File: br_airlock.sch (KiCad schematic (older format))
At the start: 23 parts, among them P1 Digital, P2 Analog, P3 CONN_01X01, P4 CONN_01X01, P5 CONN_01X01, P6 CONN_01X01

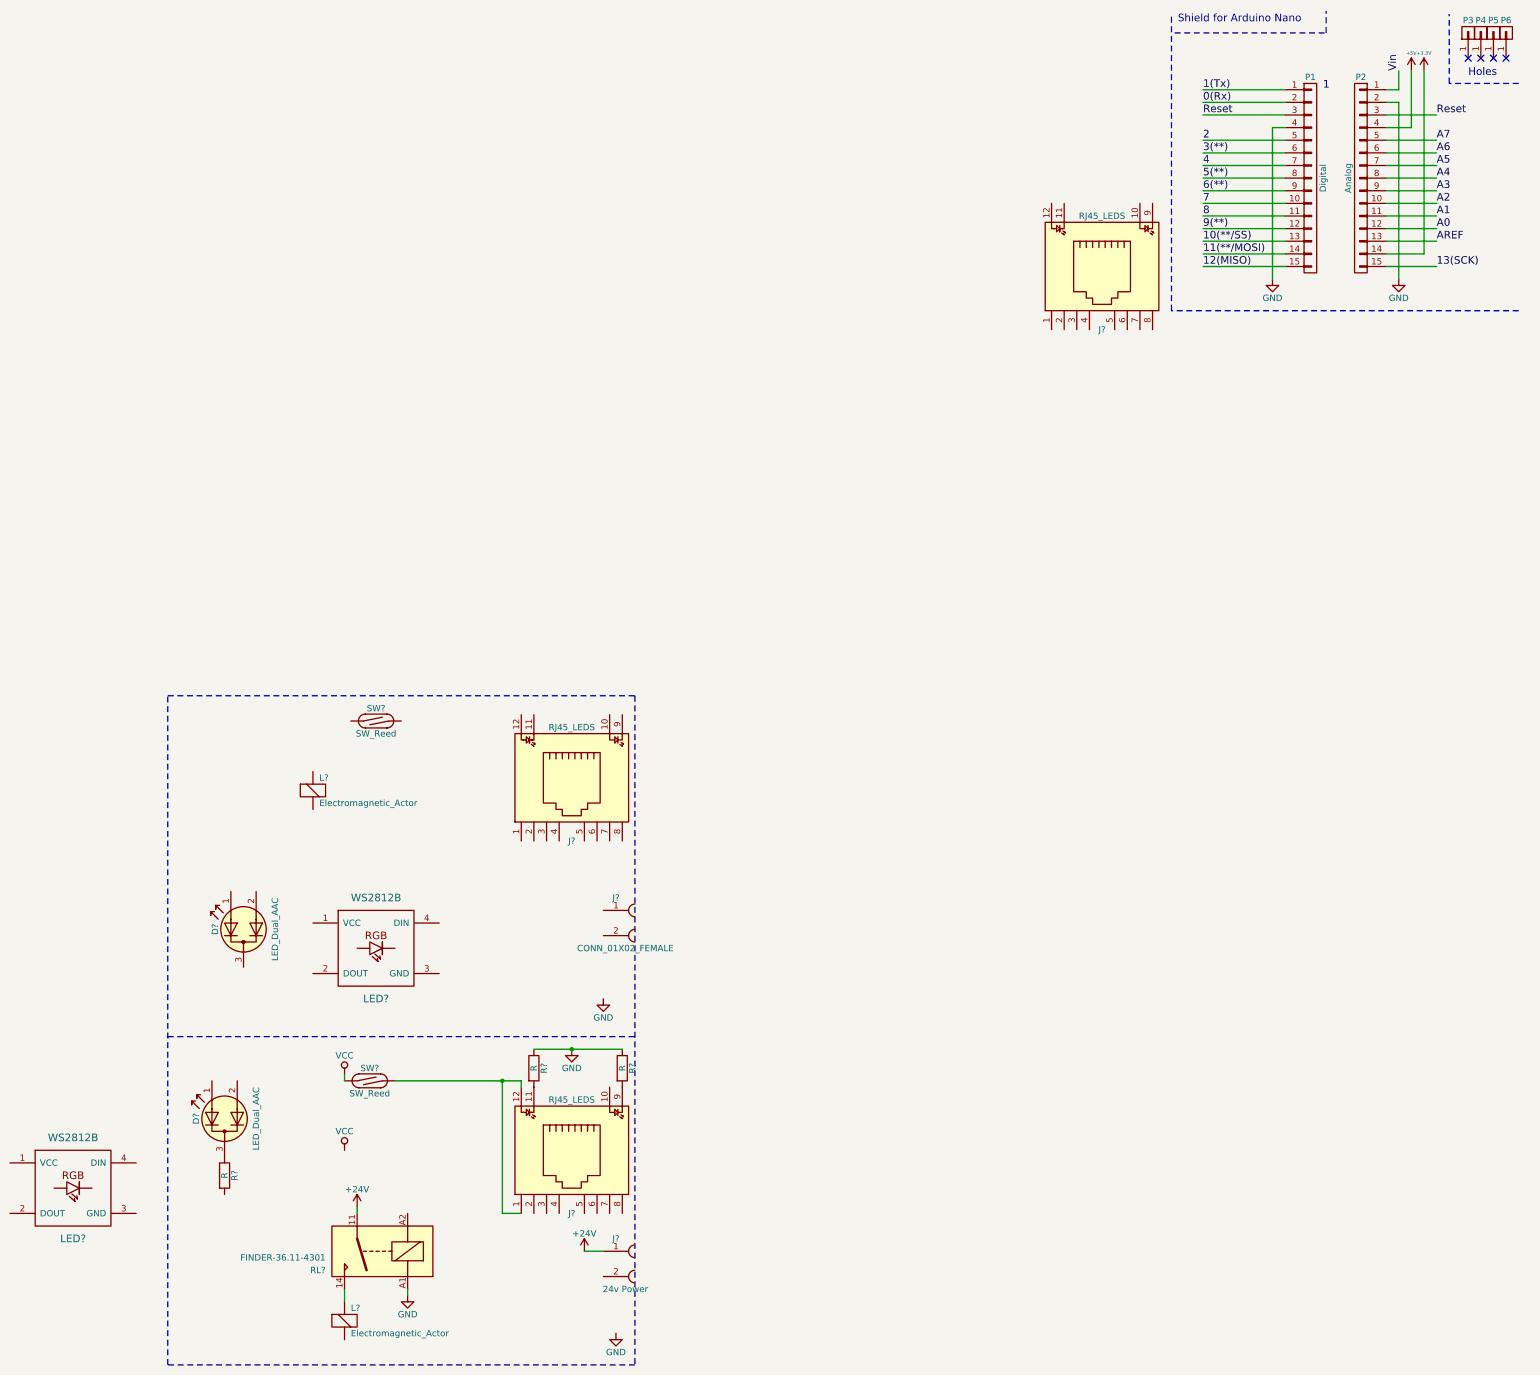
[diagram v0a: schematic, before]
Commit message: More additions. Thinking I'm running out of pins on the RJ45s, might look into a simple i/o expander.
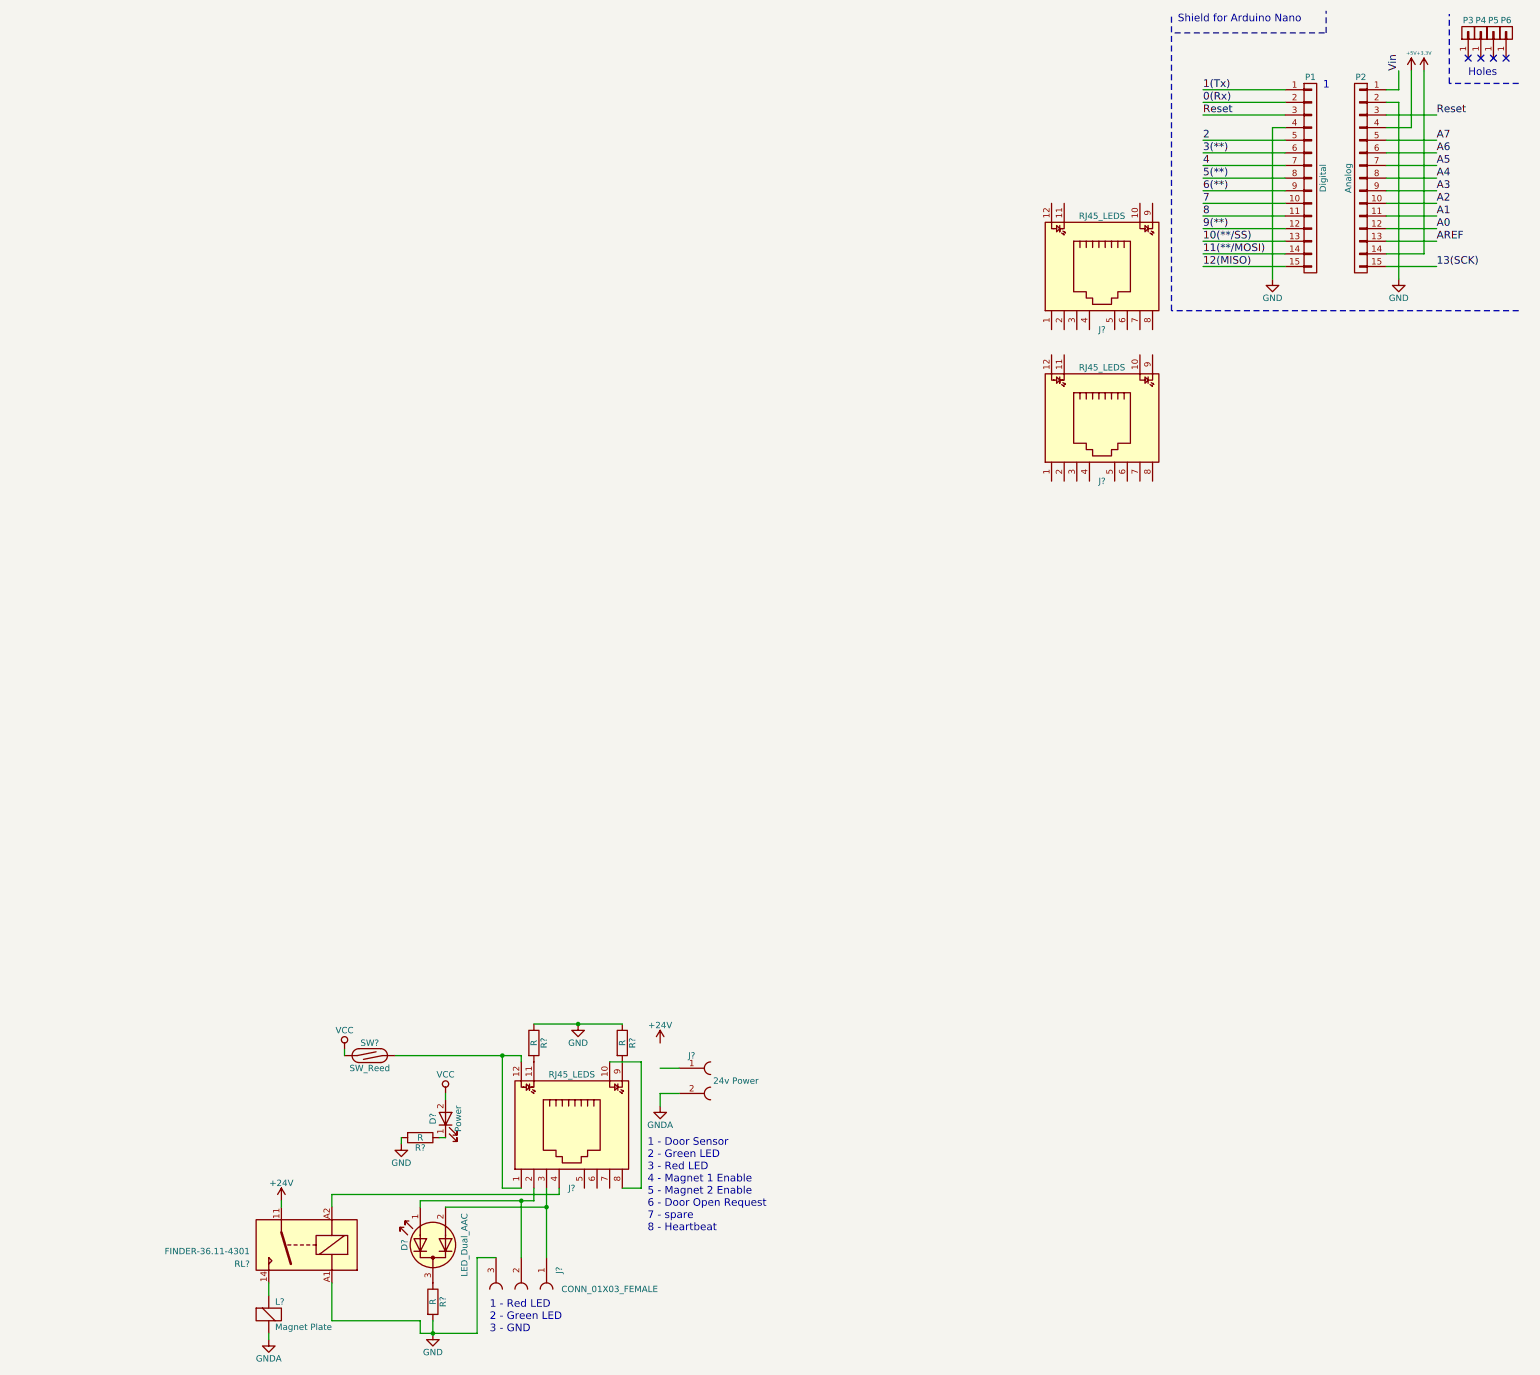
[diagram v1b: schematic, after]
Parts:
- removed D?: LED_Dual_AAC, symbol LED_Dual_AAC
- removed J?: RJ45_LEDS, symbol RJ45_LEDS
- removed J?: CONN_01X02_FEMALE, symbol CONN_01X02_FEMALE
- removed L?: Electromagnetic_Actor, symbol Electromagnetic_Actor
- removed LED? (x2): WS2812B, symbol WS2812B
- removed SW?: SW_Reed, symbol SW_Reed
- added D?: Power, symbol LED
- added J?: RJ45_LEDS, symbol RJ45_LEDS
- added J?: CONN_01X03_FEMALE, symbol CONN_01X03_FEMALE
- added R?: R, symbol R
- L?: value Electromagnetic_Actor -> Magnet Plate
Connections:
- net +24V: no longer J?.1
- net GND: now also R?.2, J?.3, R?.2
- net VCC: now also D?.2 (A)
- net GNDA: now reaches L?.2 (+)
- net GNDA: now also J?.2
- net at J?.10: now also J?.8
- net at J?.2: now also D?.1 (A1), J?.2
- net at J?.3: now also D?.2 (A2), J?.1
- net at J?.4: now also RL?.A2
- new net: D?.1 (K), R?.1
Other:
- note added: "1 - Door Sensor\n2 - Green LED\n3 - Red LED\n4 - Magnet 1 Enable\n5 - Magnet 2 Enable\n6 - Door Open Request\n7 - spare\n8 - Heartbeat"
- note added: "1 - Red LED\n2 - Green LED\n3 - GND"
- moved on the sheet: D?, J?, L?, R?, RL?, SW?

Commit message: Switched to a PCF8754 I/O Expander. Kinda wanted to always play with one.
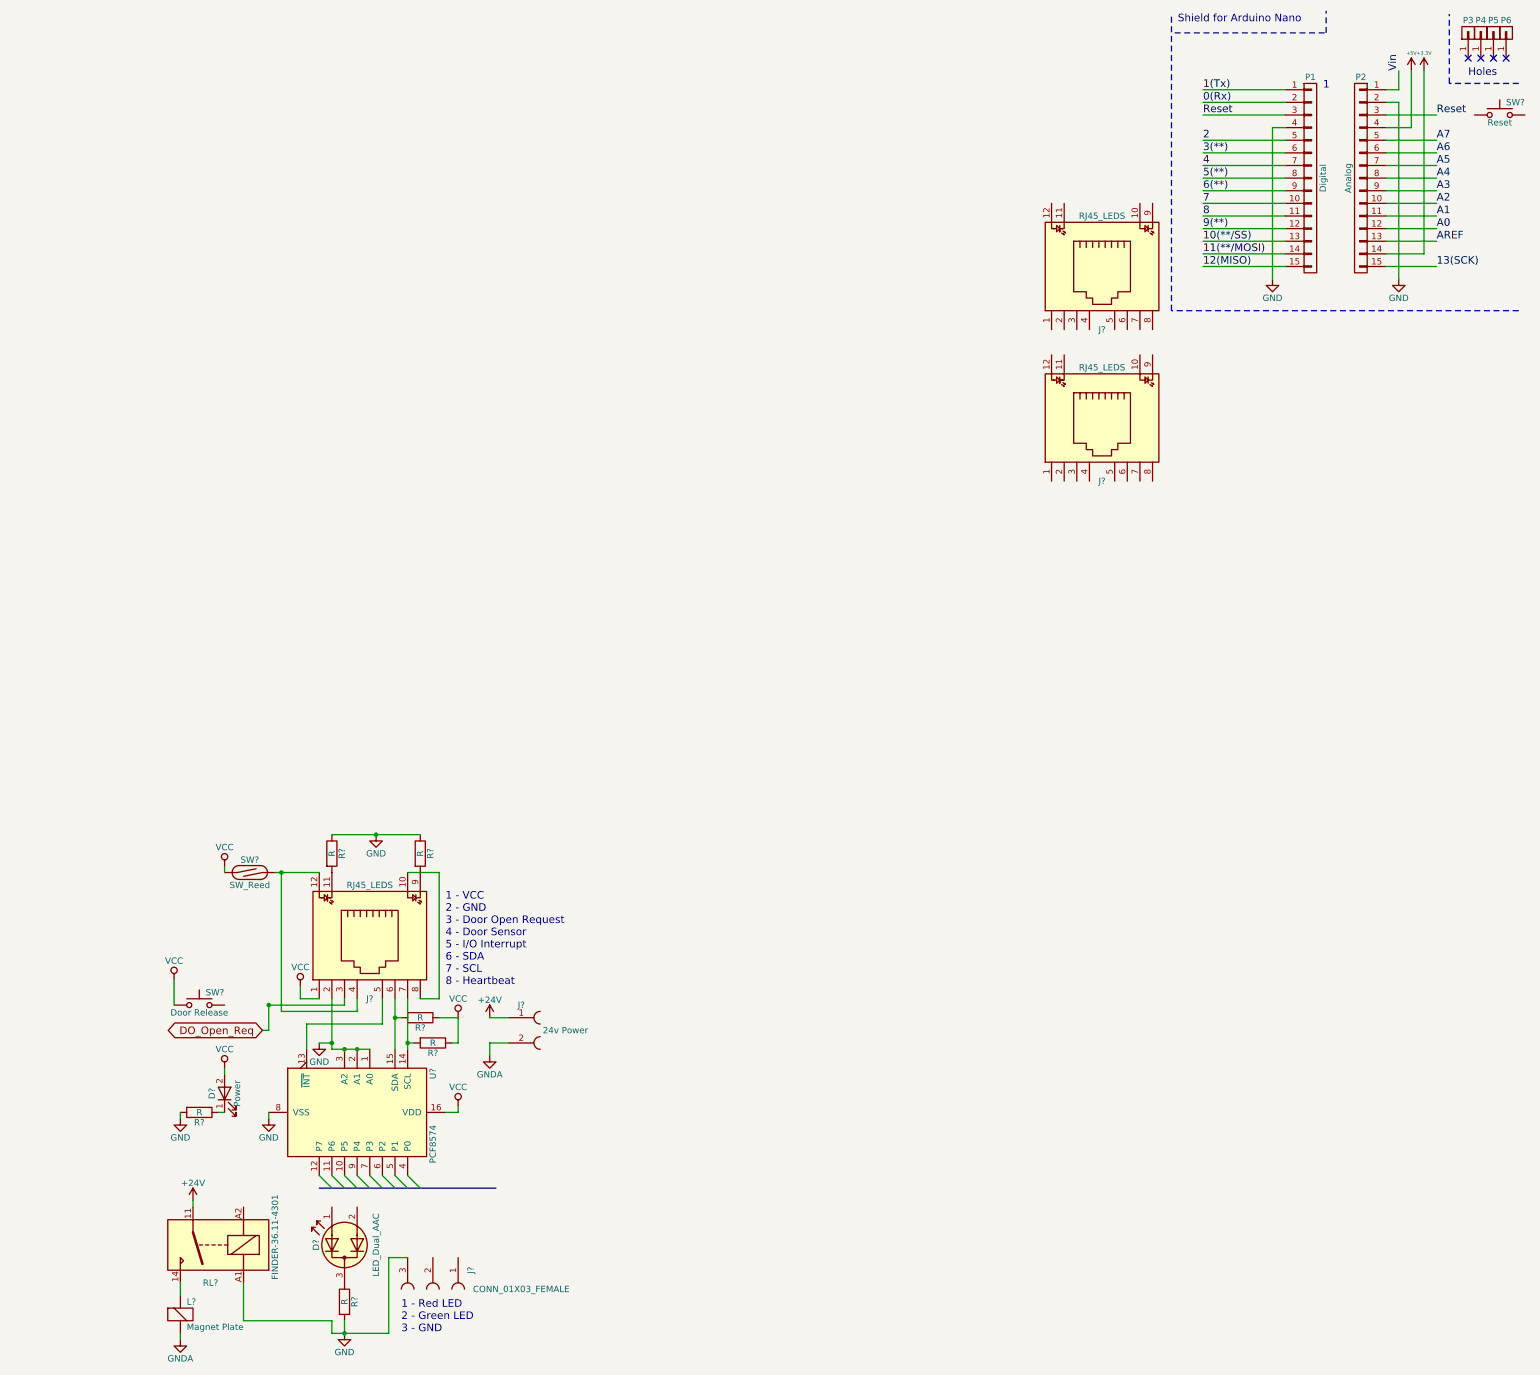
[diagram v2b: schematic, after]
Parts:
- added R? (x2): R, symbol R
- added SW?: Door Release, symbol SW_Push
- added SW?: Reset, symbol SW_Push
- added U?: PCF8574, symbol PCF8574
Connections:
- net +24V: now also J?.1
- net GND: now also J?.2, U?.1 (A0), U?.2 (A1), U?.3 (A2), U?.8 (VSS)
- net VCC: now also J?.1, R?.1, R?.1, SW?.1, U?.16 (VDD)
- net at J?.12, SW?.2: now also J?.4; no longer J?.1
- net at RL?.A2: no longer J?.4
- net at J?.5: now also U?.13 (~INT~)
- net at J?.6: now also R?.2, U?.15 (SDA)
- net at J?.7: now also R?.2, U?.14 (SCL)
- new net DO_Open_Req: J?.3
- now unconnected: D?.1 (A1), D?.2 (A2), J?.1, J?.2
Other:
- note added: "1 - VCC\n2 - GND\n3 - Door Open Request\n4 - Door Sensor\n5 - I/O Interrupt\n6 - SDA\n7 - SCL\n8 - Heartbeat"
- note removed: "1 - Door Sensor\n2 - Green LED\n3 - Red LED\n4 - Magnet 1 Enable\n5 - Magnet 2 Enable\n6 - Door Open Request\n7 - spare\n8 - Heartbeat"
- moved on the sheet: D?, J?, L?, R?, RL?, SW?

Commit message: More work. Relay needs looking at, and a VERY rough visualisation of a PCB
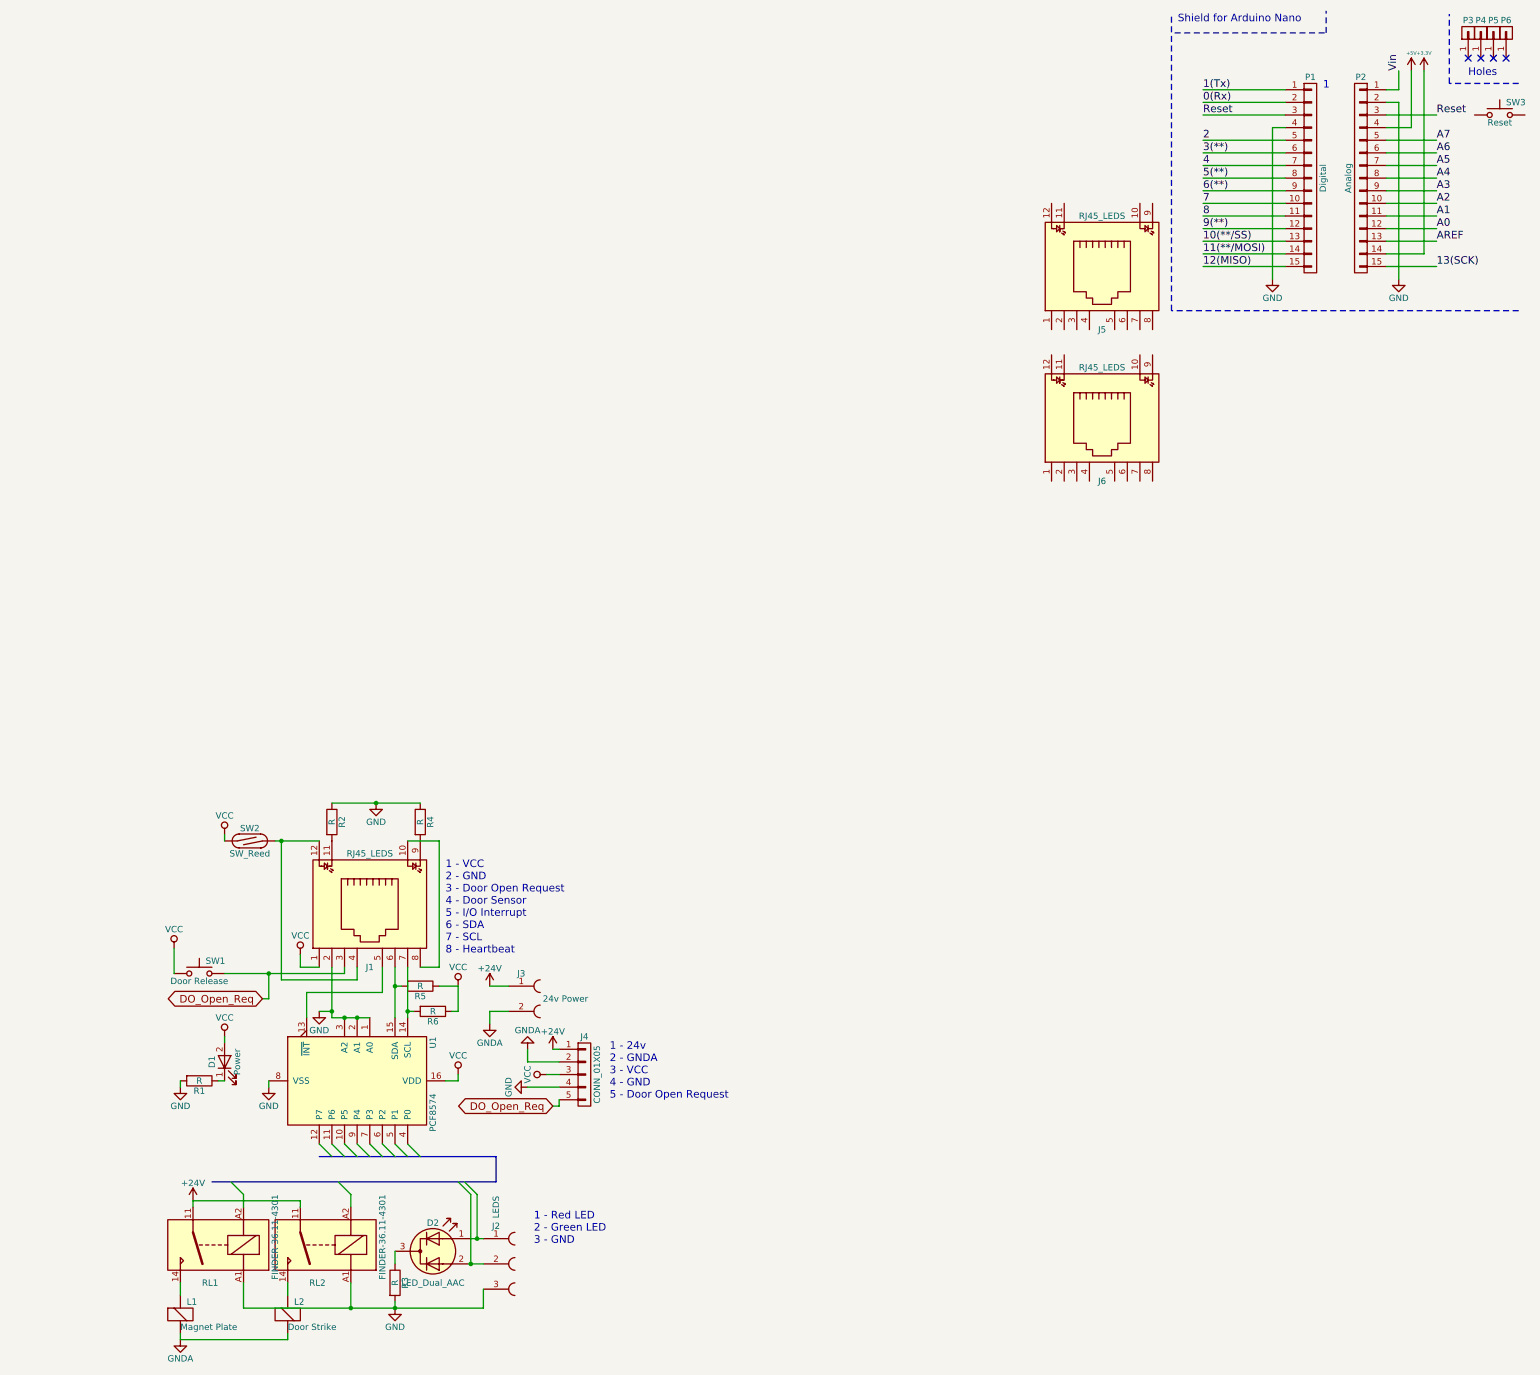
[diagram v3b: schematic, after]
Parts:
- added J4: CONN_01X05, Pin_Headers:Pin_Header_Straight_1x05_Pitch2.54mm, symbol CONN_01X05
- added L2: Door Strike, Connectors_Phoenix:PhoenixContact_MC-G_02x5.08mm_Angled, symbol Electromagnetic_Actor
- added RL2: FINDER-36.11-4301, Relays_THT:Relay_SPDT_Schrack-RP-II-1_RM3-5mm, symbol FINDER-36.11-4301
- D1: renamed from D?; footprint (none) -> LEDs:LED_0805
- D2: renamed from D?; footprint (none) -> Connectors:PINHEAD1-3
- J1, J5, J6: renamed from J?; footprint (none) -> Connectors:RJ45_8
- J2: renamed from J?; value CONN_01X03_FEMALE -> LEDS; footprint (none) -> Connectors_Terminal_Blocks:TerminalBlock_Pheonix_PT-3.5mm_3pol
- J3: renamed from J?; footprint (none) -> Connectors_Phoenix:PhoenixContact_MC-G_02x3.50mm_Angled
- L1: renamed from L?; footprint (none) -> Connectors_Phoenix:PhoenixContact_MC-G_02x5.08mm_Angled
- R1, R2, R3, R4, R5, R6: renamed from R?; footprint (none) -> Resistors_SMD:R_0805_HandSoldering
- RL1: renamed from RL?; footprint (none) -> Relays_THT:Relay_SPDT_Schrack-RP-II-1_RM3-5mm
- SW1, SW3: renamed from SW?; footprint (none) -> Buttons_Switches_THT:SW_PUSH
- SW2: renamed from SW?; footprint (none) -> Connectors_Phoenix:PhoenixContact_MC-G_02x5.08mm_Angled
- U1: renamed from U?; footprint (none) -> Housings_SOIC:SOIC-16_3.9x9.9mm_Pitch1.27mm
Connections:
- net +24V: now also J4.1 (P1), RL2.11
- net DO_Open_Req: now also SW1.2, J4.5 (P5)
- net GND: now also J4.4 (P4), RL2.A1
- net GNDA: now also J4.2 (P2), L2.2 (+)
- net VCC: now also J4.3 (P3)
- net at D2.1 (A1): now also J2.1
- net at D2.2 (A2): now also J2.2
- new net: L2.1 (-), RL2.14
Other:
- note added: "1 - 24v\n2 - GNDA\n3 - VCC\n4 - GND\n5 - Door Open Request"
- moved on the sheet: D1, D2, J1, J2, J3, R1, R2, R3, R4, R5, R6, SW1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
